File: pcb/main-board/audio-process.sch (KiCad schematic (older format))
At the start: 17 parts, among them J6 AUDIO_HEADER_OUT, J7 AUDIO_HEADER_IN, U2 LM358_BIG, U3 LM358_BIG

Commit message: working on finding components for parts
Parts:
- removed C10, C8: 100nF, ~, symbol C-rgb
- removed C11, C9: 10uF, ~, symbol CP
- added C? (x2): 10uF, ~, symbol CP-rgb
- added C? (x2): 100nF, ~, symbol C-rgb
- J6: value AUDIO_HEADER_OUT -> INPUT_JACK; Manufacturer (none) -> CUI Inc; Order (none) -> No; Product code (none) -> SJ1-3523NG; Product description (none) -> 3.50mm (0.141\", 1/8\", Mini Plug) - Headphone Phone Jack S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; Supplier (none) -> Digikey; Supplier URL (none) -> http://www.digikey.co.uk/product-detail/en/cui-inc/SJ1-3523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; Supplier code (none) -> CP1-3523NG-ND
- J7: value AUDIO_HEADER_IN -> OUTPUT_JACK; Manufacturer (none) -> CUI Inc; Order (none) -> No; Product code (none) -> SJ1-3523NG; Product description (none) -> 3.50mm (0.141\", 1/8\", Mini Plug) - Headphone Phone Jack S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; Supplier (none) -> Digikey; Supplier URL (none) -> http://www.digikey.co.uk/product-detail/en/cui-inc/SJ1-3523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; Supplier code (none) -> CP1-3523NG-ND
- renumbered C12 to C11, C13 to C12, R7 to R10, R8 to R11, R2 to R12, R4 to R6, R6 to R7, R3 to R8, R5 to R9, U3 to U2, U2 to U3
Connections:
- net +12V: now also C?.1, C?.1
- net AGND: now also U3.3 (NON_INV), C?.1, C?.1; no longer U3.5 (NON_INV)
- net AUDIO: now also U3.1 (OUT); no longer U3.7 (OUT)
- net GND: now also C?.2, C?.2, C?.2, C?.2
- net at C12.2, R7.1: now also U2.5 (NON_INV); no longer U2.3 (NON_INV)
- net at R12.1, R8.2, R9.2: now also U3.2 (INV); no longer U3.6 (INV)
- new net: R9.1, U2.6 (INV), U2.7 (OUT)

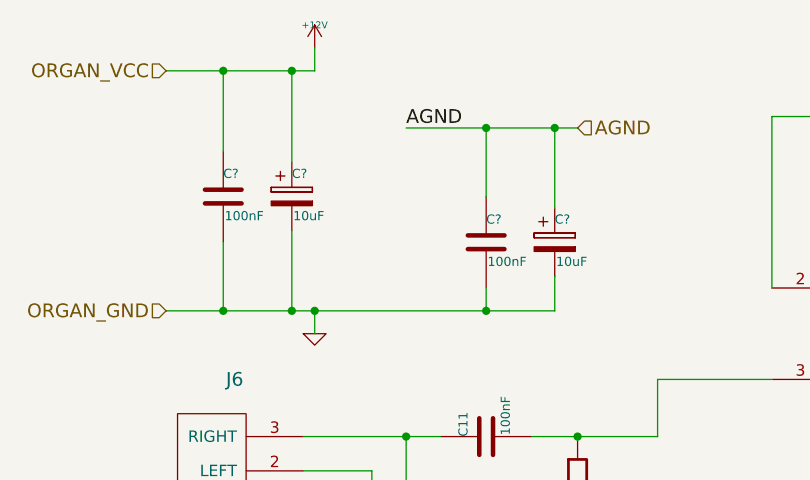
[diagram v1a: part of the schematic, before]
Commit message: finished choosing components for main board
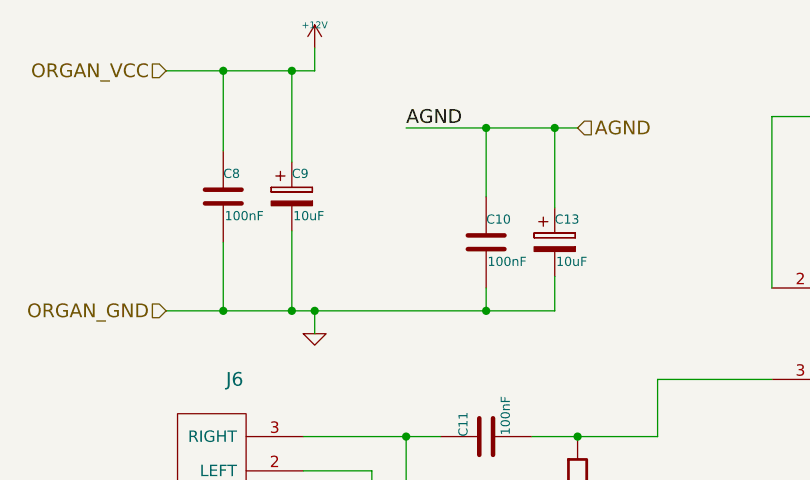
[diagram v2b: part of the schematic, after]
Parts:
- C11, C12: Manufacturer Multicomp -> Kemet; Order (none) -> No; Product code MC0805Y104M500A2.54MM -> C315C104M5U5TA; Product description Multilayer Ceramic Capacitor, MC Series, 0.1 µF, ± 20%, Y5V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 -> 0.10µF 50V Ceramic Capacitor Z5U Radial 0.150\" L x 0.100\"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; Supplier Farnell -> Digikey; Supplier code 2112751 -> 399-4151-ND
- R10, R11, R8, R9: Manufacturer (none) -> Stackpole Electronics Inc.; Order (none) -> No; Product code (none) -> CF18JT10K0; Product description (none) -> RES 10K OHM 1/8W 5% CF AXIAL; Supplier (none) -> Digikey; Supplier URL (none) -> http://www.digikey.co.uk/product-detail/en/stackpole-electr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; Supplier code (none) -> CF18JT10K0CT-ND
- R12: Manufacturer (none) -> Stackpole Electronics Inc.; Order (none) -> No; Product code (none) -> CF18JT33K0; Product description (none) -> RES 33K OHM 1/8W 5% CF AXIAL; Supplier (none) -> Digikey; Supplier URL (none) -> http://www.digikey.co.uk/product-detail/en/stackpole-electr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; Supplier code (none) -> CF18JT33K0CT-ND
- R6, R7: Manufacturer (none) -> Stackpole Electronics Inc.; Order (none) -> No; Product code (none) -> CF18JT1M00; Product description (none) -> RES 1M OHM 1/8W 5% CARBON FILM; Supplier (none) -> Digikey; Supplier URL (none) -> http://www.digikey.co.uk/product-detail/en/stackpole-electr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; Supplier code (none) -> CF18JT1M00TR-ND
- U2, U3: Manufacturer (none) -> Texas Instruments; Order (none) -> No; Product code (none) -> LM358P; Product description (none) -> General Purpose Amplifier 2 Circuit 8-PDIP; Supplier (none) -> Digikey; Supplier URL (none) -> http://www.digikey.co.uk/product-detail/en/texas-instrument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; Supplier code (none) -> 296-1395-5-ND
- gave numbers to parts that had none: 4

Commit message: misc. changes
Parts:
- J6: value INPUT_JACK -> AUDIO_JACK; Product description 3.50mm (0.141\", 1/8\", Mini Plug) - Headphone Phone Jack S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 -> 3.50mm (0.141\" 1/8\" Mini Plug) - Headphone Phone Jack Ste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
- J7: value OUTPUT_JACK -> AUDIO_JACK; Product description 3.50mm (0.141\", 1/8\", Mini Plug) - Headphone Phone Jack S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 -> 3.50mm (0.141\" 1/8\" Mini Plug) - Headphone Phone Jack Ste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
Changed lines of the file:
@@
 ORGAN_GND
 $Comp
-L GND-rgb #PWR23
+L GND-rgb #PWR022
 U 1 1 551EC9A1
 P 2050 2300
-F 0 "#PWR23" H 2050 2300 30  0001 C CNN
+F 0 "#PWR022" H 2050 2300 30  0001 C CNN
 F 1 "GND-rgb" H 2050 2230 30  0001 C CNN
 F 2 "" H 2050 2300 60  0000 C CNN
@@
 $EndComp
 $Comp
-L +12V #PWR22
+L +12V #PWR023
 U 1 1 551EC9B0
 P 2050 1050
-F 0 "#PWR22" H 2050 1000 20  0001 C CNN
+F 0 "#PWR023" H 2050 1000 20  0001 C CNN
 F 1 "+12V" H 2050 1150 30  0000 C CNN
 F 2 "" H 2050 1050 60  0000 C CNN
@@
 $EndComp
 $Comp
-L +12V #PWR31
+L +12V #PWR024
 U 1 1 551ECB9F
 P 7350 4250
-F 0 "#PWR31" H 7350 4200 20  0001 C CNN
+F 0 "#PWR024" H 7350 4200 20  0001 C CNN
 F 1 "+12V" H 7350 4350 30  0000 C CNN
 F 2 "" H 7350 4250 60  0000 C CNN
@@
 $EndComp
 $Comp
-L GND-rgb #PWR32
+L GND-rgb #PWR025
 U 1 1 551ECBA5
 P 7350 6000
-F 0 "#PWR32" H 7350 6000 30  0001 C CNN
+F 0 "#PWR025" H 7350 6000 30  0001 C CNN
 F 1 "GND-rgb" H 7350 5930 30  0001 C CNN
 F 2 "" H 7350 6000 60  0000 C CNN
@@
 P 1700 2900
 F 0 "J6" H 1700 2500 60  0000 C CNN
-F 1 "INPUT_JACK" H 1800 3250 60  0000 C CNN
+F 1 "AUDIO_JACK" H 1800 3250 60  0000 C CNN
 F 2 "" H 1700 2650 60  0000 C CNN
 F 3 "" H 1700 2650 60  0000 C CNN
 F 4 "CUI Inc" H 1700 2900 60  0001 C CNN "Manufacturer"
-F 5 "3.50mm (0.141\", 1/8\", Mini Plug) - Headphone Phone Jack Stereo Connector Solder" H 1700 2900 60  0001 C CNN "Product description"
+F 5 "3.50mm (0.141\" 1/8\" Mini Plug) - Headphone Phone Jack Stereo Connector Solder" H 1700 2900 60  0001 C CNN "Product description"
 F 6 "SJ1-3523NG" H 1700 2900 60  0001 C CNN "Product code"
 F 7 "Digikey" H 1700 2900 60  0001 C CNN "Supplier"
@@
 $EndComp
 $Comp
-L GND-rgb #PWR28
+L GND-rgb #PWR026
 U 1 1 551ED0A5
 P 4700 5050
-F 0 "#PWR28" H 4700 5050 30  0001 C CNN
+F 0 "#PWR026" H 4700 5050 30  0001 C CNN
 F 1 "GND-rgb" H 4700 4980 30  0001 C CNN
 F 2 "" H 4700 5050 60  0000 C CNN
@@
 $EndComp
 $Comp
-L +12V #PWR27
+L +12V #PWR027
 U 1 1 551ED0E3
 P 4700 3500
-F 0 "#PWR27" H 4700 3450 20  0001 C CNN
+F 0 "#PWR027" H 4700 3450 20  0001 C CNN
 F 1 "+12V" H 4700 3600 30  0000 C CNN
 F 2 "" H 4700 3500 60  0000 C CNN
@@
 $EndComp
 $Comp
-L GND-rgb #PWR26
+L GND-rgb #PWR028
 U 1 1 551ED113
 P 4700 2950
-F 0 "#PWR26" H 4700 2950 30  0001 C CNN
+F 0 "#PWR028" H 4700 2950 30  0001 C CNN
 F 1 "GND-rgb" H 4700 2880 30  0001 C CNN
 F 2 "" H 4700 2950 60  0000 C CNN
@@
 $EndComp
 $Comp
-L +12V #PWR29
+L +12V #PWR029
 U 1 1 551EE16A
 P 7350 1750
-F 0 "#PWR29" H 7350 1700 20  0001 C CNN
+F 0 "#PWR029" H 7350 1700 20  0001 C CNN
 F 1 "+12V" H 7350 1850 30  0000 C CNN
 F 2 "" H 7350 1750 60  0000 C CNN
@@
 $EndComp
 $Comp
-L GND-rgb #PWR30
+L GND-rgb #PWR030
 U 1 1 551EE17A
 P 7350 3250
-F 0 "#PWR30" H 7350 3250 30  0001 C CNN
+F 0 "#PWR030" H 7350 3250 30  0001 C CNN
 F 1 "GND-rgb" H 7350 3180 30  0001 C CNN
 F 2 "" H 7350 3250 60  0000 C CNN
@@
 AGND
 $Comp
-L GND-rgb #PWR24
+L GND-rgb #PWR031
 U 1 1 552A61C3
 P 2150 4450
-F 0 "#PWR24" H 2150 4450 30  0001 C CNN
+F 0 "#PWR031" H 2150 4450 30  0001 C CNN
 F 1 "GND-rgb" H 2150 4380 30  0001 C CNN
 F 2 "" H 2150 4450 60  0000 C CNN
@@
 	3200 4350 3200 4550
 $Comp
-L +12V #PWR25
+L +12V #PWR032
 U 1 1 5532D55C
 P 4700 1600
-F 0 "#PWR25" H 4700 1550 20  0001 C CNN
+F 0 "#PWR032" H 4700 1550 20  0001 C CNN
 F 1 "+12V" H 4700 1700 30  0000 C CNN
 F 2 "" H 4700 1600 60  0000 C CNN
@@
 	3100 1400 3100 1750
 Connection ~ 3100 1400
-$Comp
-L AUDIO_HEADER J7
-U 1 1 5808E0D8
-P 1700 3850
-F 0 "J7" H 1700 3450 60  0000 C CNN
-F 1 "OUTPUT_JACK" H 1800 4200 60  0000 C CNN
-F 2 "" H 1700 3600 60  0000 C CNN
-F 3 "" H 1700 3600 60  0000 C CNN
-F 4 "CUI Inc" H 1700 3850 60  0001 C CNN "Manufacturer"
-F 5 "3.50mm (0.141\", 1/8\", Mini Plug) - Headphone Phone Jack Stereo Connector Solder" H 1700 3850 60  0001 C CNN "Product description"
-F 6 "SJ1-3523NG" H 1700 3850 60  0001 C CNN "Product code"
-F 7 "Digikey" H 1700 3850 60  0001 C CNN "Supplier"
-F 8 "CP1-3523NG-ND" H 1700 3850 60  0001 C CNN "Supplier code"
-F 9 "No" H 1700 3850 60  0001 C CNN "Order"
-F 10 "http://www.digikey.co.uk/product-detail/en/cui-inc/SJ1-3523NG/CP1-3523NG-ND/738692" H 1700 3850 60  0001 C CNN "Supplier URL"
-	1    1700 3850
-	-1   0    0    1
-$EndComp
 $Comp
 L CP-rgb C9
@@
 	1    0    0    -1
 $EndComp
+$Comp
+L AUDIO_HEADER J7
+U 1 1 5814040E
+P 1700 3850
+F 0 "J7" H 1700 3450 60  0000 C CNN
+F 1 "AUDIO_JACK" H 1800 4200 60  0000 C CNN
+F 2 "" H 1700 3600 60  0000 C CNN
+F 3 "" H 1700 3600 60  0000 C CNN
+F 4 "CUI Inc" H 1700 3850 60  0001 C CNN "Manufacturer"
+F 5 "3.50mm (0.141\" 1/8\" Mini Plug) - Headphone Phone Jack Stereo Connector Solder" H 1700 3850 60  0001 C CNN "Product description"
+F 6 "SJ1-3523NG" H 1700 3850 60  0001 C CNN "Product code"
+F 7 "Digikey" H 1700 3850 60  0001 C CNN "Supplier"
+F 8 "CP1-3523NG-ND" H 1700 3850 60  0001 C CNN "Supplier code"
+F 9 "No" H 1700 3850 60  0001 C CNN "Order"
+F 10 "http://www.digikey.co.uk/product-detail/en/cui-inc/SJ1-3523NG/CP1-3523NG-ND/738692" H 1700 3850 60  0001 C CNN "Supplier URL"
+	1    1700 3850
+	-1   0    0    1
+$EndComp
 $EndSCHEMATC
